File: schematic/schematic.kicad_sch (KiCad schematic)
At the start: 5 parts, among them J1 Conn_01x19, J2 Conn_01x19, P1 外部給電コネクタ, SW1 電源選択スイッチ

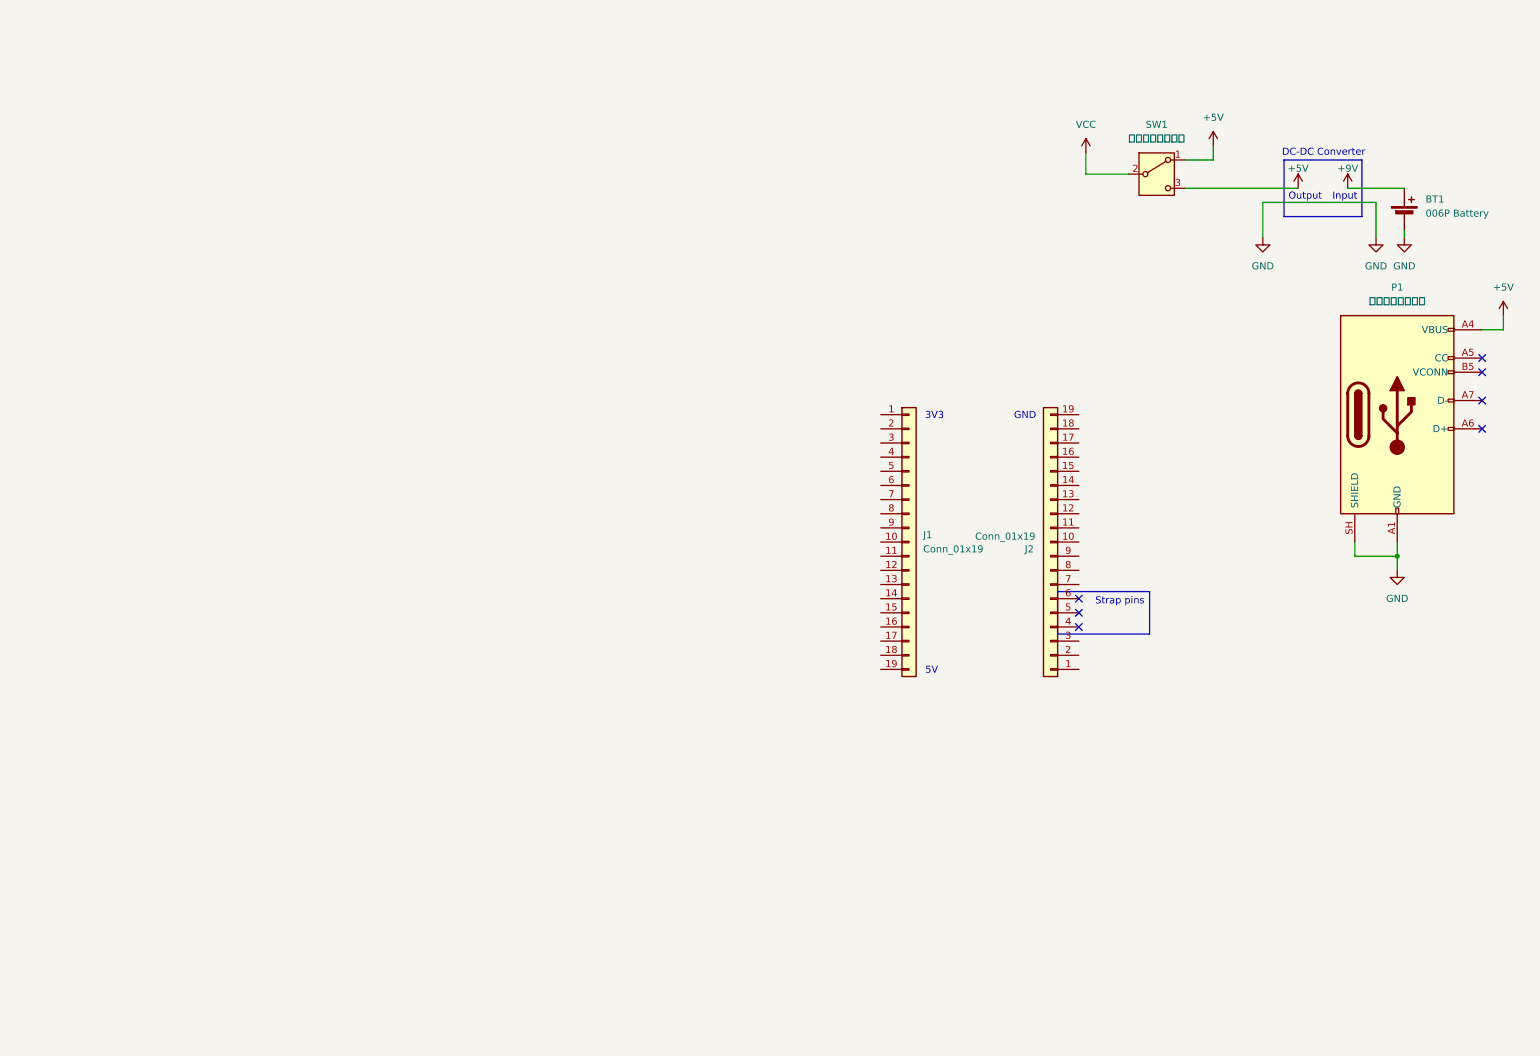
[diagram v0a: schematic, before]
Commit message: Added some parts to schematic
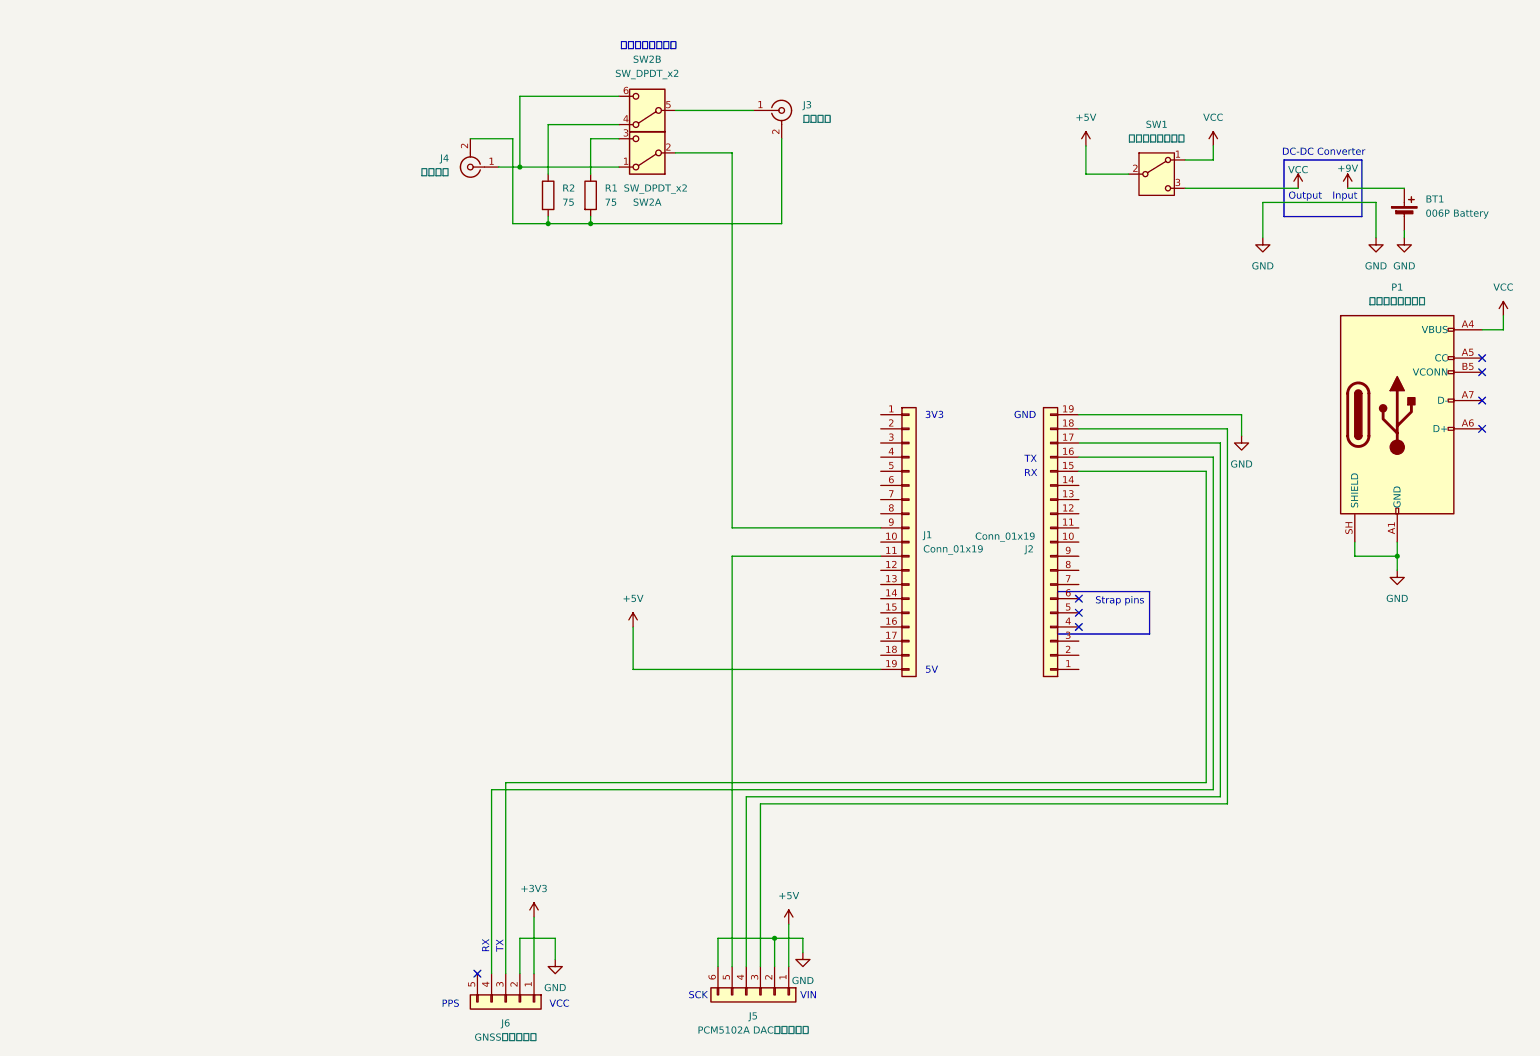
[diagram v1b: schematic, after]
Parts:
- added J3: 映像入力, symbol Connector:Conn_Coaxial
- added J4: 映像出力, symbol Connector:Conn_Coaxial
- added J5: PCM5102A DACモジュール, symbol Connector_Generic:Conn_01x06
- added J6: GNSSモジュール, symbol Connector_Generic:Conn_01x05
- added R1, R2: 75, symbol Device:R
- added SW2: SW_DPDT_x2, symbol Switch:SW_DPDT_x2
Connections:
- net +5V: now also J1.19 (Pin_19), SW1.2 (B), J5.1 (Pin_1); no longer P1.A4 (VBUS), P1.A9 (VBUS), P1.B4 (VBUS), P1.B9 (VBUS), SW1.1 (A), SW1.3 (C)
- net GND: now also J2.19 (Pin_19), J5.2 (Pin_2), J5.6 (Pin_6), J6.2 (Pin_2)
- net VCC: now also P1.A4 (VBUS), P1.A9 (VBUS), P1.B4 (VBUS), P1.B9 (VBUS), SW1.1 (A), SW1.3 (C); no longer SW1.2 (B)
- net at J1.11 (Pin_11): now also J5.5 (Pin_5)
- net at J1.9 (Pin_9): now also SW2.2 (B)
- net at J2.15 (Pin_15): now also J6.3 (Pin_3)
- net at J2.16 (Pin_16): now also J6.4 (Pin_4)
- net at J2.17 (Pin_17): now also J5.4 (Pin_4)
- net at J2.18 (Pin_18): now also J5.3 (Pin_3)
- new net: R2.1, SW2.4 (A)
- new net: J3.2 (Ext), J4.2 (Ext), R1.2, R2.2
- new net: R1.1, SW2.3 (C)
- new net: J4.1 (In), SW2.1 (A), SW2.6 (C)
- new net: J3.1 (In), SW2.5 (B)
- new net +3V3: J6.1 (Pin_1)
- no-connect marks 7 -> 8
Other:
- note added: "PPS"
- note added: "RX"
- note added: "SCK"
- note added: "TX"
- note added: "VCC"
- note added: "VIN"
- note added: "映像選択スイッチ"

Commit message: Added LCD and TF card slot
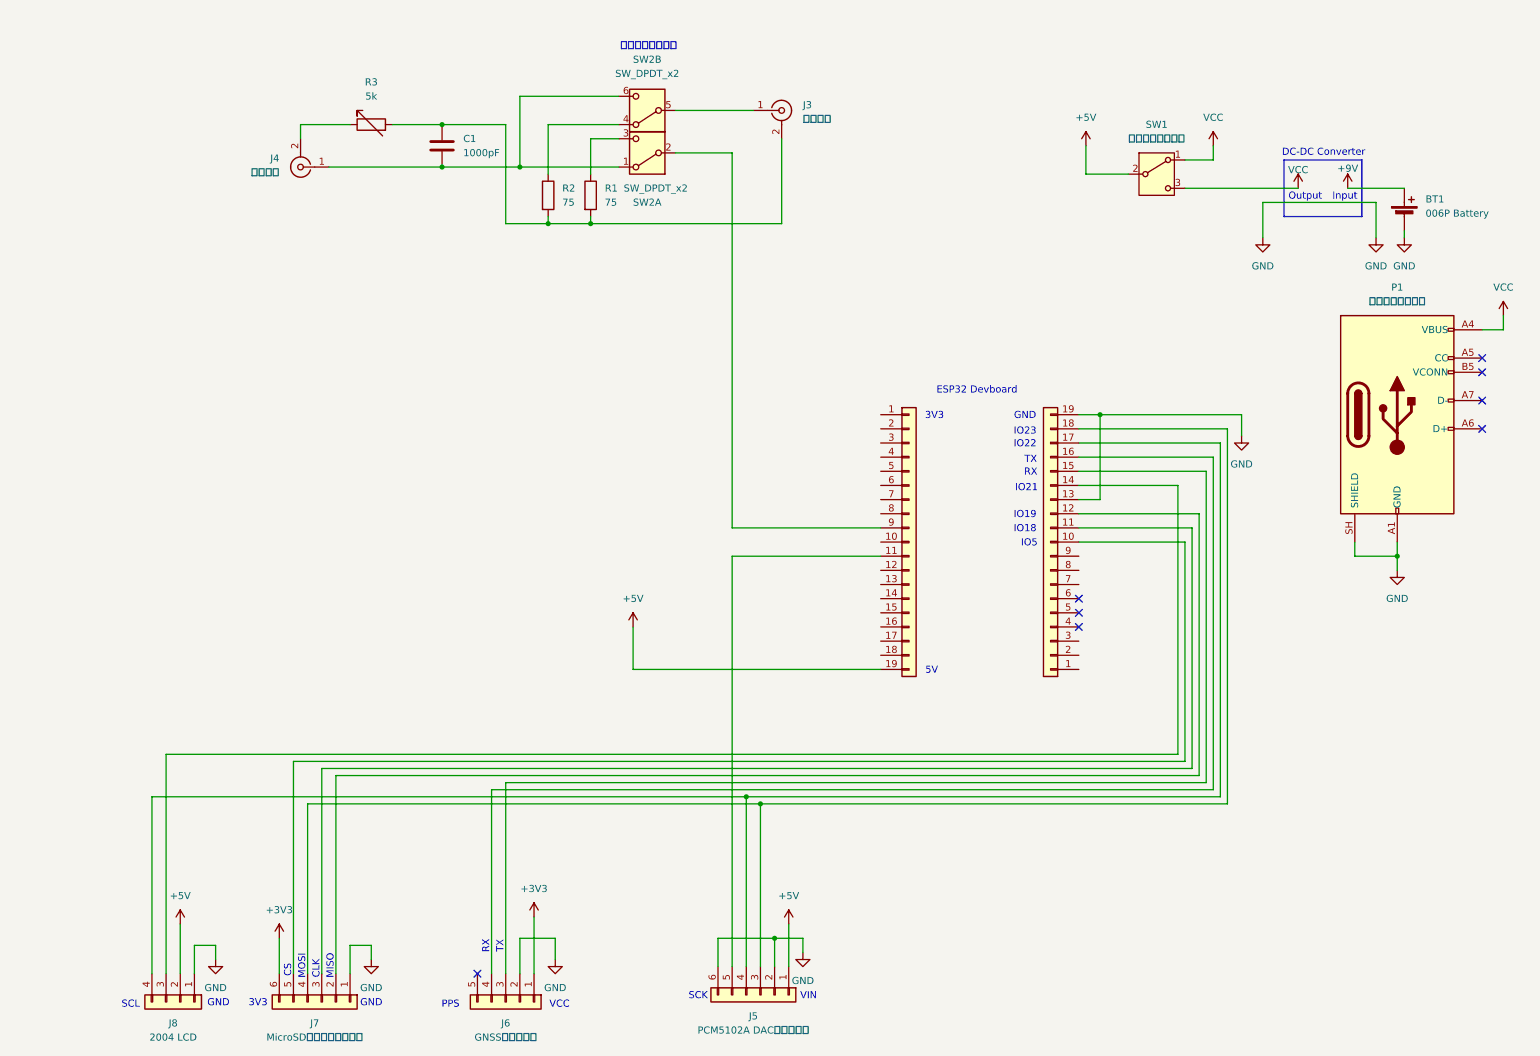
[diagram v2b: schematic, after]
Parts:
- added C1: 1000pF, symbol Device:C
- added J7: MicroSDカードモジュール, symbol Connector_Generic:Conn_01x06
- added J8: 2004 LCD, symbol Connector_Generic:Conn_01x04
- added R3: 5k, symbol Device:R_Variable
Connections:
- net +3V3: now also J7.6 (Pin_6)
- net +5V: now also J8.2 (Pin_2)
- net GND: now also J2.13 (Pin_13), J7.1 (Pin_1), J8.1 (Pin_1)
- net at J3.2 (Ext), R1.2, R2.2: now also C1.1, R3.2; no longer J4.2 (Ext)
- net at J2.10 (Pin_10): now also J7.5 (Pin_5)
- net at J2.11 (Pin_11): now also J7.3 (Pin_3)
- net at J2.12 (Pin_12): now also J7.2 (Pin_2)
- net at J2.14 (Pin_14): now also J8.3 (Pin_3)
- net at J2.17 (Pin_17), J5.4 (Pin_4): now also J8.4 (Pin_4)
- net at J2.18 (Pin_18), J5.3 (Pin_3): now also J7.4 (Pin_4)
- net at J4.1 (In), SW2.1 (A), SW2.6 (C): now also C1.2
- new net: J4.2 (Ext), R3.1
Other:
- note added: "CLK"
- note added: "CS"
- note added: "ESP32 Devboard"
- note added: "IO18"
- note added: "IO19"
- note added: "IO21"
- note added: "IO22"
- note added: "IO23"
- note added: "IO5"
- note added: "MISO"
- note added: "MOSI"
- note added: "SCL"
- note removed: "Strap pins"
- moved on the sheet: J4

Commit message: Added rotary encoder and other components
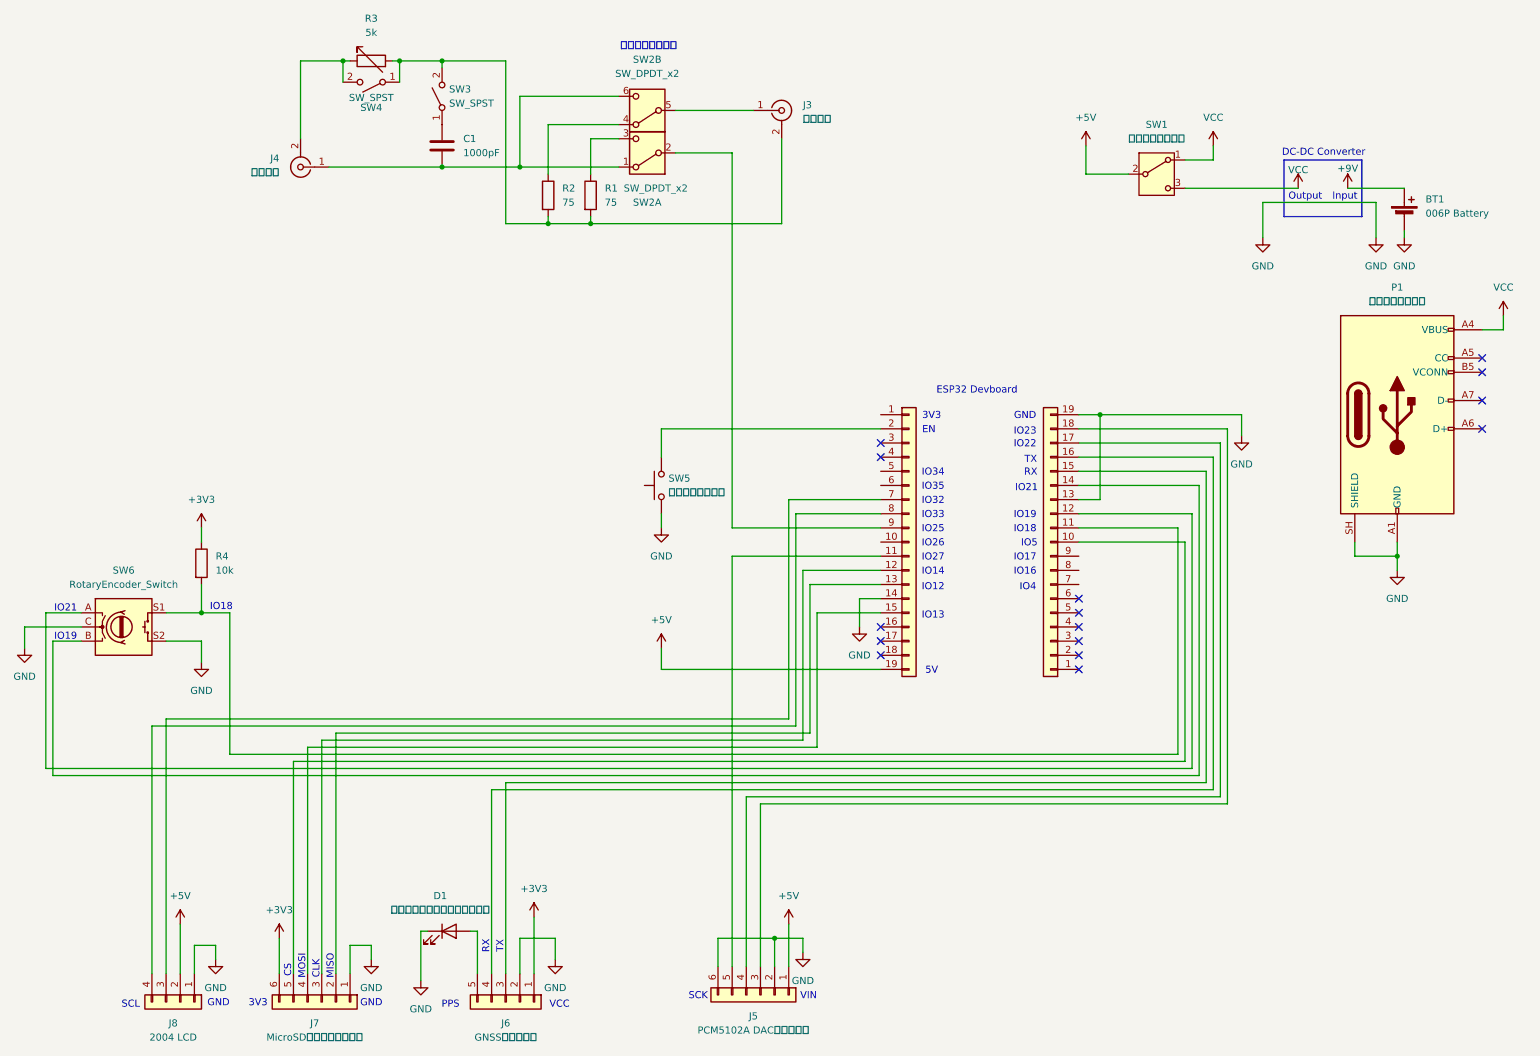
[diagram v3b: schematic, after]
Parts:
- added D1: 衛星捕捉インジケーターランプ, symbol Device:LED
- added R4: 10k, symbol Device:R
- added SW3, SW4: SW_SPST, symbol Switch:SW_SPST
- added SW5: リセットスイッチ, symbol Switch:SW_Push
- added SW6: RotaryEncoder_Switch, symbol Device:RotaryEncoder_Switch
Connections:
- net +3V3: now also R4.1
- net GND: now also J1.14 (Pin_14), D1.1 (K), SW5.1, SW6.C, SW6.S2
- net at J3.2 (Ext), R1.2, R2.2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: now also SW3.2 (B), SW4.1 (A); no longer C1.1
- net at J1.12 (Pin_12): now also J7.3 (Pin_3)
- net at J1.13 (Pin_13): now also J7.2 (Pin_2)
- net at J1.15 (Pin_15): now also J7.4 (Pin_4)
- net at J1.2 (Pin_2): now also SW5.2
- net at J1.7 (Pin_7): now also J8.3 (Pin_3)
- net at J1.8 (Pin_8): now also J8.4 (Pin_4)
- net at J2.11 (Pin_11): now also R4.2, SW6.S1; no longer J7.3 (Pin_3)
- net at J2.12 (Pin_12): now also SW6.A; no longer J7.2 (Pin_2)
- net at J2.14 (Pin_14): now also SW6.B; no longer J8.3 (Pin_3)
- net at J2.17 (Pin_17), J5.4 (Pin_4): no longer J8.4 (Pin_4)
- net at J2.18 (Pin_18), J5.3 (Pin_3): no longer J7.4 (Pin_4)
- net at J4.2 (Ext), R3.1: now also SW4.2 (B)
- net at J6.5 (Pin_5): now also D1.2 (A)
- new net: C1.1, SW3.1 (A)
- no-connect marks 8 -> 15
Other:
- note added: "EN"
- note added: "IO12"
- note added: "IO13"
- note added: "IO14"
- note added: "IO16"
- note added: "IO17"
- note added: "IO25"
- note added: "IO26"
- note added: "IO27"
- note added: "IO32"
- note added: "IO33"
- note added: "IO34"
- note added: "IO35"
- note added: "IO4"
- moved on the sheet: R3
